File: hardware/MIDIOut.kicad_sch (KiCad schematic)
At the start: 6 parts, among them J201 SJ2-25404B-SMT-TR, U201 74AHC1G125

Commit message: Refresh
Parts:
- D201: Manufacturer (none) -> ROHM Semiconductor; Mouser (none) -> 755-RB501SM-30FHT2R; Product (none) -> RB501SM-30FHT2R
- J201: Manufacturer (none) -> Same Sky; Mouser (none) -> 490-SJ2-25404BSMT-TR; Product (none) -> SJ2-25404B-SMT-TR
- TVS201: Manufacturer (none) -> Bourns; Mouser (none) -> 652-CG0603MLC-05LE; Product (none) -> CG0603MLC-05LE; Rating (none) -> 5V
- U201: Manufacturer (none) -> Texas Instruments; Mouser (none) -> 595-SN74AHC1G125DBVR; Product (none) -> SN74AHC1G125DBVR
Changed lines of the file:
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@@
+			)
+		)
+		(property "Mouser" "755-RB501SM-30FHT2R"
+			(at 170.18 96.52 0)
+			(effects
+				(font
+					(size 1.27 1.27)
+				)
+				(hide yes)
+			)
+		)
+		(property "Product" "RB501SM-30FHT2R"
+			(at 167.64 96.52 0)
+			(effects
+				(font
+					(size 1.27 1.27)
+				)
+				(hide yes)
+			)
+		)
+		(property "Manufacturer" "ROHM Semiconductor"
+			(at 165.1 96.52 0)
+			(effects
+				(font
+					(size 1.27 1.27)
+				)
+				(hide yes)
 			)
 		)
@@
 		(property "Description" "Single Buffer Gate Tri-State, Low-Voltage CMOS"
 			(at 105.41 109.22 0)
+			(effects
+				(font
+					(size 1.27 1.27)
+				)
+				(hide yes)
+			)
+		)
+		(property "Mouser" "595-SN74AHC1G125DBVR"
+			(at 105.41 137.16 0)
+			(effects
+				(font
+					(size 1.27 1.27)
+				)
+				(hide yes)
+			)
+		)
+		(property "Product" "SN74AHC1G125DBVR"
+			(at 105.41 134.62 0)
+			(effects
+				(font
+					(size 1.27 1.27)
+				)
+				(hide yes)
+			)
+		)
+		(property "Manufacturer" "Texas Instruments"
+			(at 105.41 132.08 0)
 			(effects
 				(font
@@
 			)
 		)
-		(property "Description" "SJ2-35464B-SMT-TR"
+		(property "Description" ""
 			(at 207.518 122.174 0)
 			(effects
@@
 				)
 				(justify left bottom)
+				(hide yes)
+			)
+		)
+		(property "Mouser" "490-SJ2-25404BSMT-TR"
+			(at 199.136 137.16 0)
+			(effects
+				(font
+					(size 1.27 1.27)
+				)
+				(hide yes)
+			)
+		)
+		(property "Product" "SJ2-25404B-SMT-TR"
+			(at 199.39 134.62 0)
+			(effects
+				(font
+					(size 1.27 1.27)
+				)
+				(hide yes)
+			)
+		)
+		(property "Manufacturer" "Same Sky"
+			(at 199.39 132.08 0)
+			(effects
+				(font
+					(size 1.27 1.27)
+				)
 				(hide yes)
 			)
@@
 			(effects
 				(font
+					(size 1.27 1.27)
+				)
+				(hide yes)
+			)
+		)
+		(property "Mouser" "652-CG0603MLC-05LE"
+			(at 133.35 113.03 0)
+			(effects
+				(font
+					(size 1.27 1.27)
+				)
+				(hide yes)
+			)
+		)
+		(property "Product" "CG0603MLC-05LE"
+			(at 128.524 113.03 0)
+			(effects
+				(font
+					(size 1.27 1.27)
+				)
+				(hide yes)
+			)
+		)
+		(property "Manufacturer" "Bourns"
+			(at 125.73 113.03 0)
+			(effects
+				(font
+					(size 1.27 1.27)
+				)
+				(hide yes)
+			)
+		)
+		(property "Rating" "5V"
+			(at 130.81 113.03 0)
+			(effects
+				(font

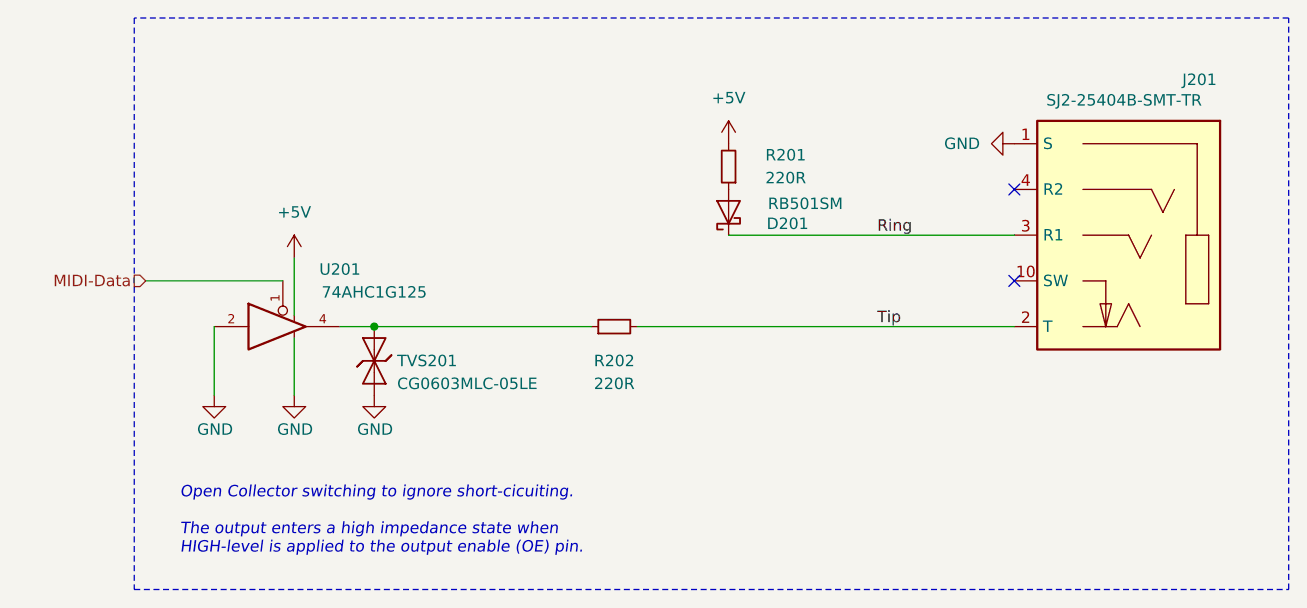
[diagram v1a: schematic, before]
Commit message: Replace Order_Number
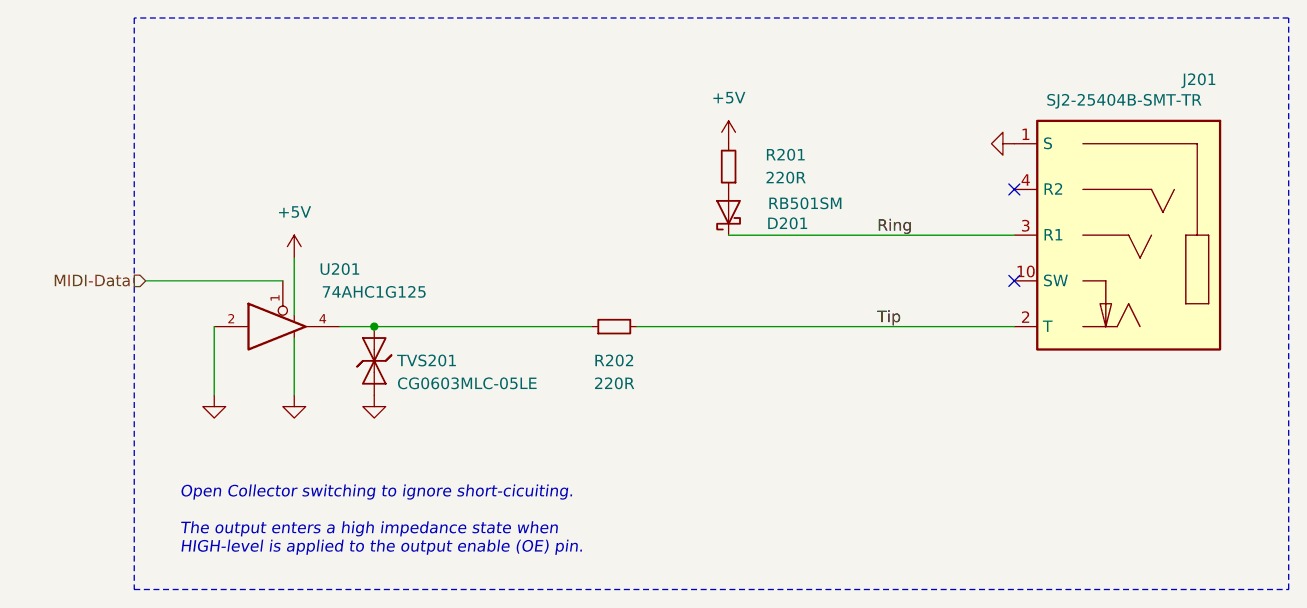
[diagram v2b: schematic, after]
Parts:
- D201: footprint Diode_SMD:D_SOD-523 -> V2_Diode_SMD:D_SOD-523
- R201, R202: footprint Resistor_SMD:R_0603_1608Metric -> V2_Resistor_SMD:R_0603; symbol Device:R_Small -> V2_Device:R_0603_220R; Manufacturer (none) -> Vishay; Mouser (none) -> 71-CRCW0603220RFKEAH; Product (none) -> CRCW0603220RFKEAHP; Rating (none) -> 330mW
- TVS201: footprint Diode_SMD:D_0603_1608Metric -> V2_Diode_SMD:D_0603
- U201: footprint Package_TO_SOT_SMD:SOT-23-5 -> V2_Package_TO_SOT_SMD:SOT-23-5
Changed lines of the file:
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@@
 	)
 	(symbol
-		(lib_id "power:GND")
+		(lib_id "V2_power:GND")
 		(at 97.79 116.84 0)
 		(unit 1)
@@
 				)
 				(justify left)
+				(hide yes)
 			)
 		)
@@
 			)
 		)
-		(property "Description" "Power symbol creates a global label with name \"GND\" , ground"
+		(property "Description" ""
 			(at 97.79 116.84 0)
 			(effects
@@
 	)
 	(symbol
-		(lib_id "power:GND")
+		(lib_id "V2_power:GND")
 		(at 115.57 116.84 0)
 		(unit 1)
@@
 				)
 				(justify left)
+				(hide yes)
 			)
 		)
@@
 			)
 		)
-		(property "Description" "Power symbol creates a global label with name \"GND\" , ground"
+		(property "Description" ""
 			(at 115.57 116.84 0)
 			(effects
@@
 	)
 	(symbol
-		(lib_id "Device:R_Small")
+		(lib_id "V2_Device:R_0603_220R")
 		(at 142.24 109.22 90)
 		(unit 1)
@@
 			)
 		)
-		(property "Footprint" "Resistor_SMD:R_0603_1608Metric"
+		(property "Footprint" "V2_Resistor_SMD:R_0603"
+			(at 157.988 109.22 0)
+			(effects
+				(font
+					(size 1.27 1.27)
+				)
+				(hide yes)
+			)
+		)
+		(property "Datasheet" ""
 			(at 142.24 109.22 0)
 			(effects
@@
 			)
 		)
-		(property "Datasheet" "~"
-			(at 142.24 109.22 0)
-			(effects
-				(font
-					(size 1.27 1.27)
-				)
-				(hide yes)
-			)
-		)
 		(property "Description" "Resistor, small symbol"
-			(at 142.24 109.22 0)
+			(at 154.94 109.22 0)
+			(effects
+				(font
+					(size 1.27 1.27)
+				)
+				(hide yes)
+			)
+		)
+		(property "Mouser" "71-CRCW0603220RFKEAH"
+			(at 165.1 109.22 0)
+			(effects
+				(font
+					(size 1.27 1.27)
+				)
+				(hide yes)
+			)
+		)
+		(property "Product" "CRCW0603220RFKEAHP"
+			(at 160.02 109.22 0)
+			(effects
+				(font
+					(size 1.27 1.27)
+				)
+				(hide yes)
+			)
+		)
+		(property "Manufacturer" "Vishay"
+			(at 157.48 109.22 0)
+			(effects
+				(font
+					(size 1.27 1.27)
+				)
+				(hide yes)
+			)
+		)
+		(property "Rating" "330mW"
+			(at 162.56 109.22 0)
 			(effects
 				(font
@@
 	)
 	(symbol
-		(lib_id "power:+5V")
+		(lib_id "V2_power:+5V")
 		(at 106.68 101.6 0)
 		(unit 1)
@@
 			)
 		)
-		(property "Description" "Power symbol creates a global label with name \"+5V\""
+		(property "Description" ""
 			(at 106.68 101.6 0)
 			(effects
@@
 	)
 	(symbol
-		(lib_id "Device:R_Small")
+		(lib_id "V2_Device:R_0603_220R")
 		(at 154.94 91.44 180)
 		(unit 1)
@@
 			)
 		)
-		(property "Footprint" "Resistor_SMD:R_0603_1608Metric"
+		(property "Footprint" "V2_Resistor_SMD:R_0603"
+			(at 154.94 75.692 0)
+			(effects
+				(font
+					(size 1.27 1.27)
+				)
+				(hide yes)
+			)
+		)
+		(property "Datasheet" ""
 			(at 154.94 91.44 0)
 			(effects
@@
 			)
 		)
-		(property "Datasheet" "~"
-			(at 154.94 91.44 0)
-			(effects
-				(font
-					(size 1.27 1.27)
-				)
-				(hide yes)
-			)
-		)
 		(property "Description" "Resistor, small symbol"
-			(at 154.94 91.44 0)
+			(at 154.94 78.74 0)
+			(effects
+				(font
+					(size 1.27 1.27)
+				)
+				(hide yes)
+			)
+		)
+		(property "Mouser" "71-CRCW0603220RFKEAH"
+			(at 154.94 68.58 0)
+			(effects
+				(font
+					(size 1.27 1.27)
+				)
+				(hide yes)
+			)
+		)
+		(property "Product" "CRCW0603220RFKEAHP"
+			(at 154.94 73.66 0)
+			(effects
+				(font
+					(size 1.27 1.27)
+				)
+				(hide yes)
+			)
+		)
+		(property "Manufacturer" "Vishay"
+			(at 154.94 76.2 0)
+			(effects
+				(font
+					(size 1.27 1.27)
+				)
+				(hide yes)
+			)
+		)
+		(property "Rating" "330mW"
+			(at 154.94 71.12 0)
 			(effects
 				(font
@@
 	)
 	(symbol
-		(lib_id "power:GND")
+		(lib_id "V2_power:GND")
 		(at 186.69 88.9 270)
 		(unit 1)
@@
 				)
 				(justify right)
+				(hide yes)
 			)
 		)
@@
 			)
 		)
-		(property "Description" "Power symbol creates a global label with name \"GND\" , ground"
+		(property "Description" ""
 			(at 186.69 88.9 0)
 			(effects
@@
 	)
 	(symbol
-		(lib_id "power:GND")
+		(lib_id "V2_power:GND")
 		(at 106.68 116.84 0)
 		(unit 1)
@@
 				)
 				(justify left)
+				(hide yes)
 			)
 		)
@@
 			)
 		)
-		(property "Description" "Power symbol creates a global label with name \"GND\" , ground"
+		(property "Description" ""
 			(at 106.68 116.84 0)
 			(effects
@@
 			)
 		)
-		(property "Footprint" "Diode_SMD:D_SOD-523"
+		(property "Footprint" "V2_Diode_SMD:D_SOD-523"
 			(at 161.925 96.52 0)
 			(effects
@@
 			)
 		)
-		(property "Footprint" "Package_TO_SOT_SMD:SOT-23-5"
+		(property "Footprint" "V2_Package_TO_SOT_SMD:SOT-23-5"
 			(at 105.41 109.22 0)
 			(effects
@@
 	)
 	(symbol
-		(lib_id "power:+5V")
+		(lib_id "V2_power:+5V")
 		(at 154.94 88.9 0)
 		(unit 1)
@@
 			)
 		)
-		(property "Description" "Power symbol creates a global label with name \"+5V\""
+		(property "Description" ""
 			(at 154.94 88.9 0)
 			(effects
@@
 			)
 		)
-		(property "Footprint" "Diode_SMD:D_0603_1608Metric"
+		(property "Footprint" "V2_Diode_SMD:D_0603"
 			(at 121.285 113.03 0)
 			(effects

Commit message: Update Library
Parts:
- R201, R202: symbol V2_Device:R_0603_220R -> V2_Resistor:0603_220R
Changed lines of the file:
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@@
 		(on_board yes)
 		(dnp no)
-		(property "Reference" "#PWR0204"
+		(property "Reference" "#PWR204"
 			(at 97.79 123.19 0)
 			(effects
@@
 			(project "radio"
 				(path "/6c8448b4-b04d-47e1-934e-e40cbe27a7be/a2a7e0b0-ac2f-4b58-a957-fda1af6d6784"
-					(reference "#PWR0204")
+					(reference "#PWR204")
 					(unit 1)
 				)
@@
 		(on_board yes)
 		(dnp no)
-		(property "Reference" "#PWR0206"
+		(property "Reference" "#PWR206"
 			(at 115.57 123.19 0)
 			(effects
@@
 			(project "radio"
 				(path "/6c8448b4-b04d-47e1-934e-e40cbe27a7be/a2a7e0b0-ac2f-4b58-a957-fda1af6d6784"
-					(reference "#PWR0206")
-					(unit 1)
-				)
-			)
-		)
-	)
-	(symbol
-		(lib_id "V2_Device:R_0603_220R")
+					(reference "#PWR206")
+					(unit 1)
+				)
+			)
+		)
+	)
+	(symbol
+		(lib_id "V2_Resistor:0603_220R")
 		(at 142.24 109.22 90)
 		(unit 1)
@@
 		(dnp no)
 		(fields_autoplaced yes)
-		(property "Reference" "#PWR0203"
+		(property "Reference" "#PWR203"
 			(at 106.68 105.41 0)
 			(effects
@@
 			(project "radio"
 				(path "/6c8448b4-b04d-47e1-934e-e40cbe27a7be/a2a7e0b0-ac2f-4b58-a957-fda1af6d6784"
-					(reference "#PWR0203")
-					(unit 1)
-				)
-			)
-		)
-	)
-	(symbol
-		(lib_id "V2_Device:R_0603_220R")
+					(reference "#PWR203")
+					(unit 1)
+				)
+			)
+		)
+	)
+	(symbol
+		(lib_id "V2_Resistor:0603_220R")
 		(at 154.94 91.44 180)
 		(unit 1)
@@
 		(dnp no)
 		(fields_autoplaced yes)
-		(property "Reference" "#PWR0202"
+		(property "Reference" "#PWR202"
 			(at 180.34 88.9 0)
 			(effects
@@
 			(project "radio"
 				(path "/6c8448b4-b04d-47e1-934e-e40cbe27a7be/a2a7e0b0-ac2f-4b58-a957-fda1af6d6784"
-					(reference "#PWR0202")
+					(reference "#PWR202")
 					(unit 1)
 				)
@@
 		(on_board yes)
 		(dnp no)
-		(property "Reference" "#PWR0205"
+		(property "Reference" "#PWR205"
 			(at 106.68 123.19 0)
 			(effects
@@
 			(project "radio"
 				(path "/6c8448b4-b04d-47e1-934e-e40cbe27a7be/a2a7e0b0-ac2f-4b58-a957-fda1af6d6784"
-					(reference "#PWR0205")
+					(reference "#PWR205")
 					(unit 1)
 				)
@@
 		(dnp no)
 		(fields_autoplaced yes)
-		(property "Reference" "#PWR0201"
+		(property "Reference" "#PWR201"
 			(at 154.94 92.71 0)
 			(effects
@@
 			(project "radio"
 				(path "/6c8448b4-b04d-47e1-934e-e40cbe27a7be/a2a7e0b0-ac2f-4b58-a957-fda1af6d6784"
-					(reference "#PWR0201")
-					(unit 1)
-				)
+					(reference "#PWR201")
+					(unit 1)
+				)

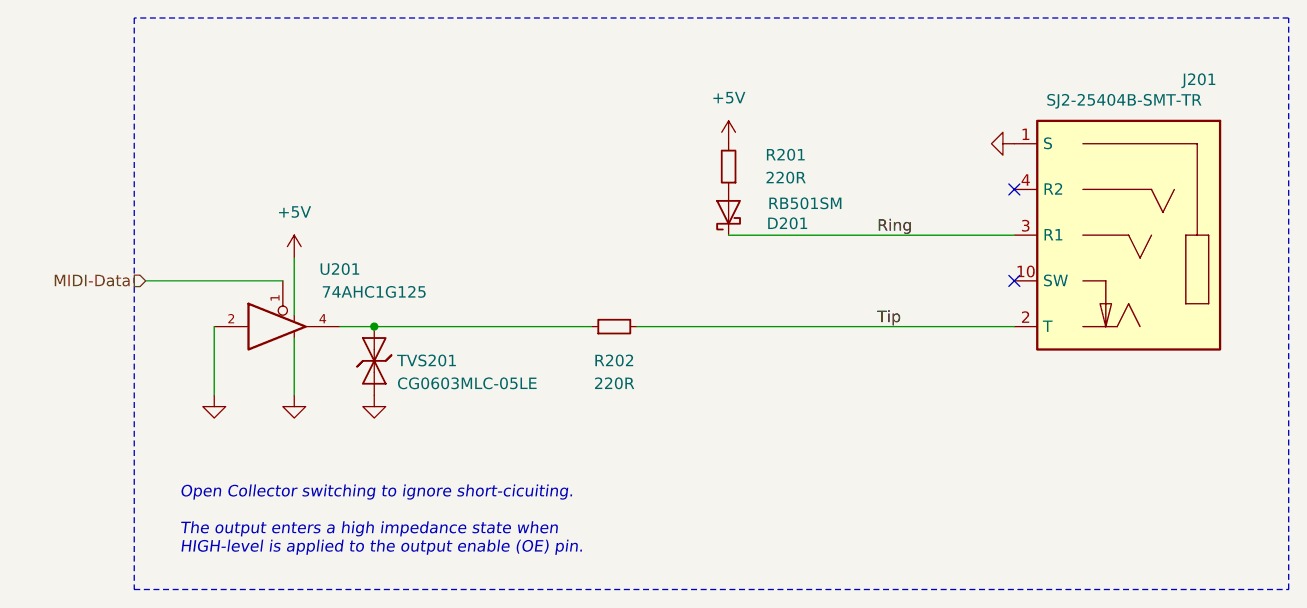
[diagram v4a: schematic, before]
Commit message: Replace diode
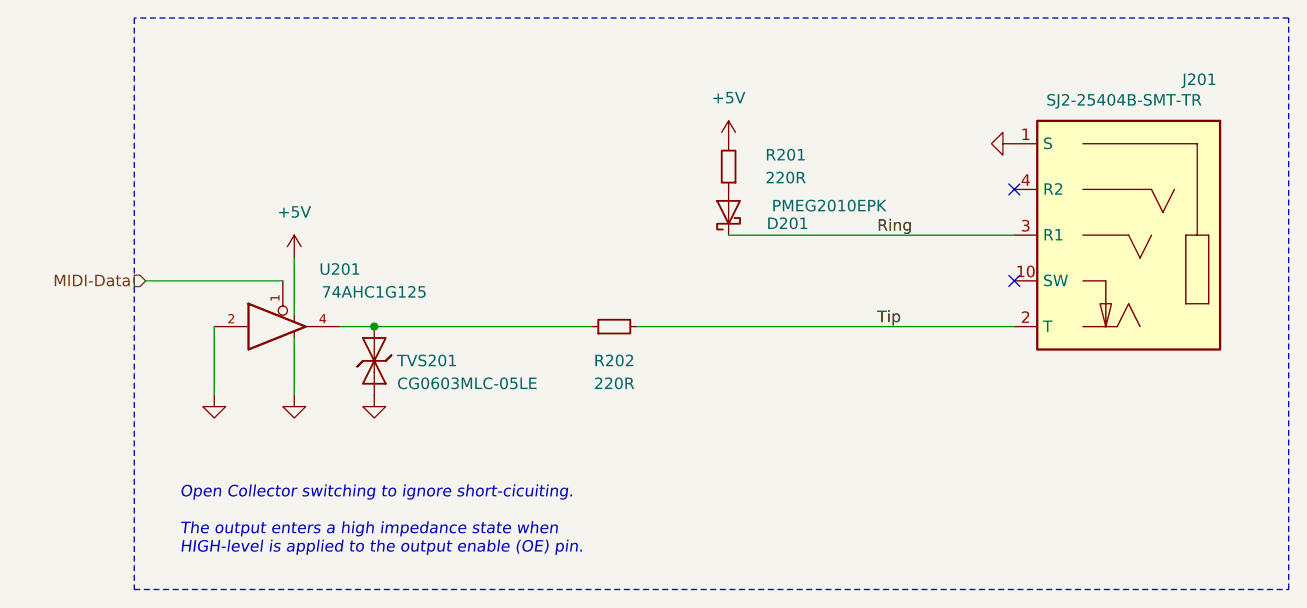
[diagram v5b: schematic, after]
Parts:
- D201: value RB501SM -> PMEG2010EPK; footprint V2_Diode_SMD:D_SOD-523 -> V2_Diode_SMD:D_SOD-1608; symbol V2_Diode:RB501SM -> V2_Diode:PMEG2010EPK; Manufacturer ROHM Semiconductor -> Nexperia; Mouser 755-RB501SM-30FHT2R -> 771-PMEG2010EPK; Product RB501SM-30FHT2R -> PMEG2010EPK; Rating (none) -> 20V
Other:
- title: MIDI Out -> V2 radio

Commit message: Update
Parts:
- added C201: 0u1, V2_Capacitor_SMD:C_0603, symbol V2_Capacitor:0603_0u1
- D201, TVS201: Id (none) -> Diode:${SYMBOL_NAME}
- J201: Id (none) -> Audio:${SYMBOL_NAME}; Rating (none) -> 2.5mm
- R201: renamed from R202; Id (none) -> Resistor:${SYMBOL_NAME}
- R202: renamed from R201; Id (none) -> Resistor:${SYMBOL_NAME}
- U201: Id (none) -> 74xGxx:${SYMBOL_NAME}; Rating (none) -> 8mA
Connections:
- net +5V: now also C201.1
- net GND: now also C201.2
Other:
- company: (none) -> Versio Duo

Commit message: Good Bye Imperial
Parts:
- C201: footprint V2_Capacitor_SMD:C_0603 -> V2_Capacitor_SMD:C_1608; symbol V2_Capacitor:0603_0u1 -> V2_Capacitor:1608_0u1
- R201, R202: footprint V2_Resistor_SMD:R_0603 -> V2_Resistor_SMD:R_1608; symbol V2_Resistor:0603_220R -> V2_Resistor:1608_220R
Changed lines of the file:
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@@
 	)
 	(symbol
-		(lib_id "V2_Capacitor:0603_0u1")
+		(lib_id "V2_Capacitor:1608_0u1")
 		(at 106.68 86.36 0)
 		(unit 1)
@@
 			)
 		)
-		(property "Footprint" "V2_Capacitor_SMD:C_0603"
+		(property "Footprint" "V2_Capacitor_SMD:C_1608"
 			(at 106.68 103.378 0)
 			(hide yes)
@@
 	)
 	(symbol
-		(lib_id "V2_Resistor:0603_220R")
+		(lib_id "V2_Resistor:1608_220R")
 		(at 142.24 109.22 90)
 		(unit 1)
@@
 			)
 		)
-		(property "Footprint" "V2_Resistor_SMD:R_0603"
+		(property "Footprint" "V2_Resistor_SMD:R_1608"
 			(at 157.988 109.22 0)
 			(hide yes)
@@
 	)
 	(symbol
-		(lib_id "V2_Resistor:0603_220R")
+		(lib_id "V2_Resistor:1608_220R")
 		(at 154.94 91.44 180)
 		(unit 1)
@@
 			)
 		)
-		(property "Footprint" "V2_Resistor_SMD:R_0603"
+		(property "Footprint" "V2_Resistor_SMD:R_1608"
 			(at 154.94 75.692 0)
 			(hide yes)
